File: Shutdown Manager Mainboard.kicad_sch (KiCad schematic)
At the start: 20 parts, among them J1 Conn_01x04, J2 Conn_01x03, J3 Conn_01x03, J6 Conn_01x03, K1 Relay_SPST_Panasonic_DJH-Form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, U1 Seeed Studio XIAO SAMD21, U2 TPS76133DBVR, U3 DRV8220DSGR, U4 DRV8220DSGR

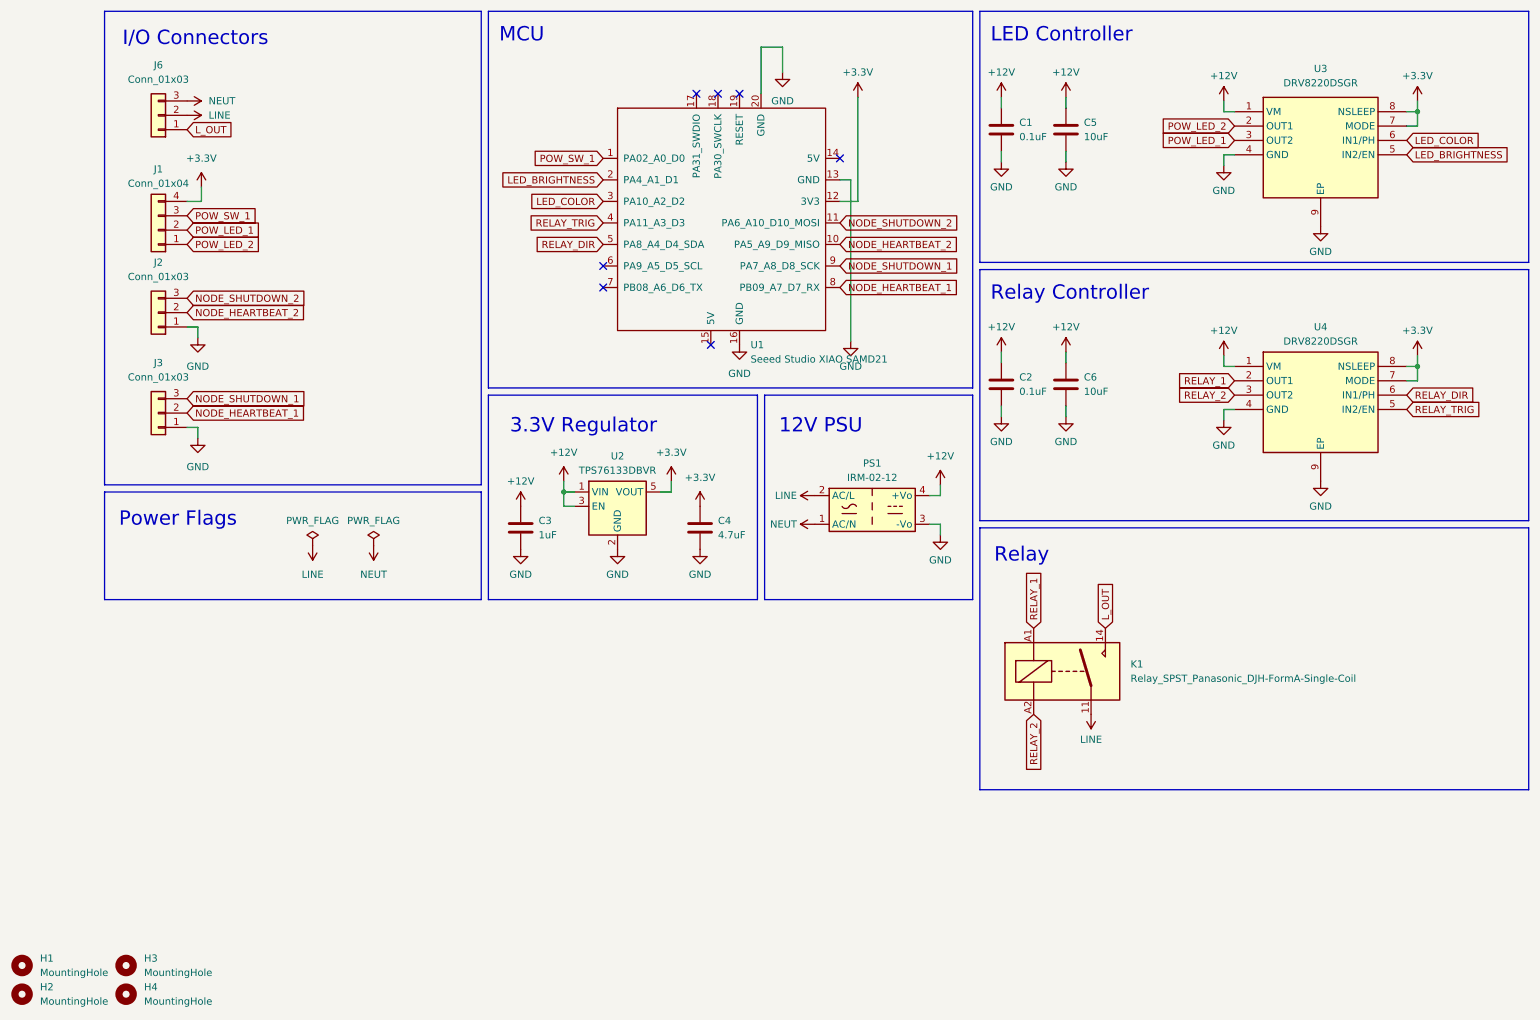
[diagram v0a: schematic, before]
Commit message: Added strong external pullup/-down resistors to inputs, Added RC filter to main power button input
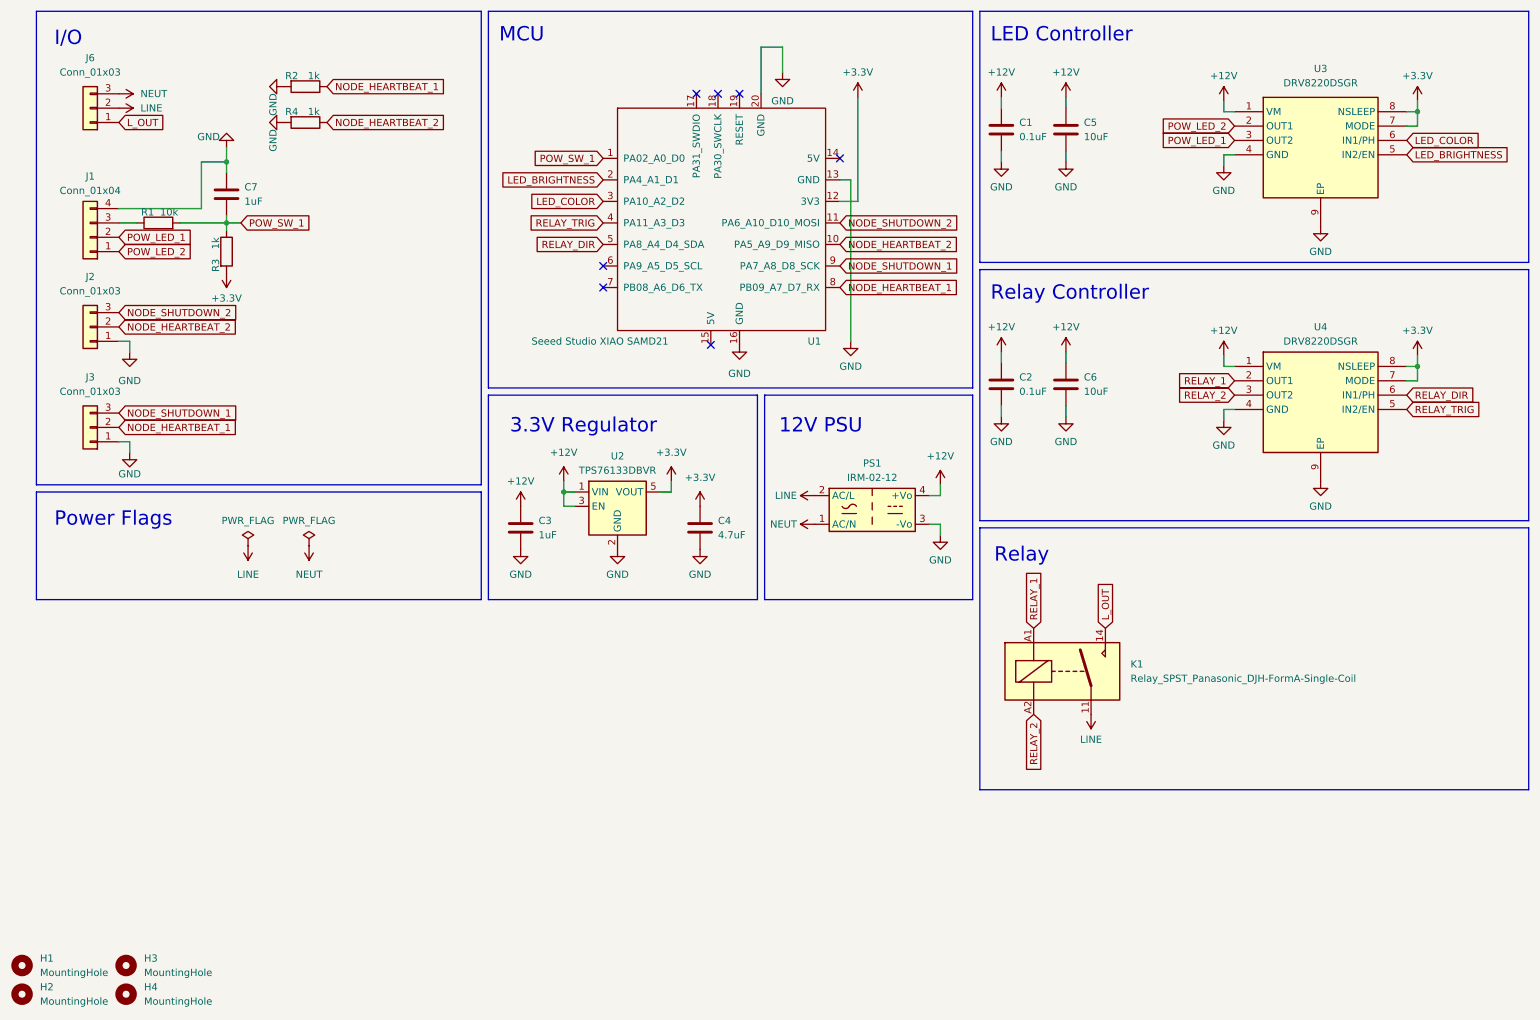
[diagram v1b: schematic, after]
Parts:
- added C7: 1uF, Capacitor_SMD:C_0402_1005Metric, symbol Device:C
- added R1: 10k, Resistor_SMD:R_0402_1005Metric, symbol Device:R
- added R2, R3, R4: 1k, Resistor_SMD:R_0402_1005Metric, symbol Device:R
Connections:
- net +3.3V: now also R3.2; no longer J1.4 (Pin_4)
- net GND: now also J1.4 (Pin_4), C7.1, R2.2, R4.2
- net NODE_HEARTBEAT_1: now also R2.1
- net NODE_HEARTBEAT_2: now also R4.1
- net POW_SW_1: now also C7.2, R1.2, R3.1; no longer J1.3 (Pin_3)
- new net: J1.3 (Pin_3), R1.1
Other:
- note added: "I/O"
- note removed: "I/O Connectors"
- moved on the sheet: J1, J2, J3, J6

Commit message: Fixed heartbeat input filtering
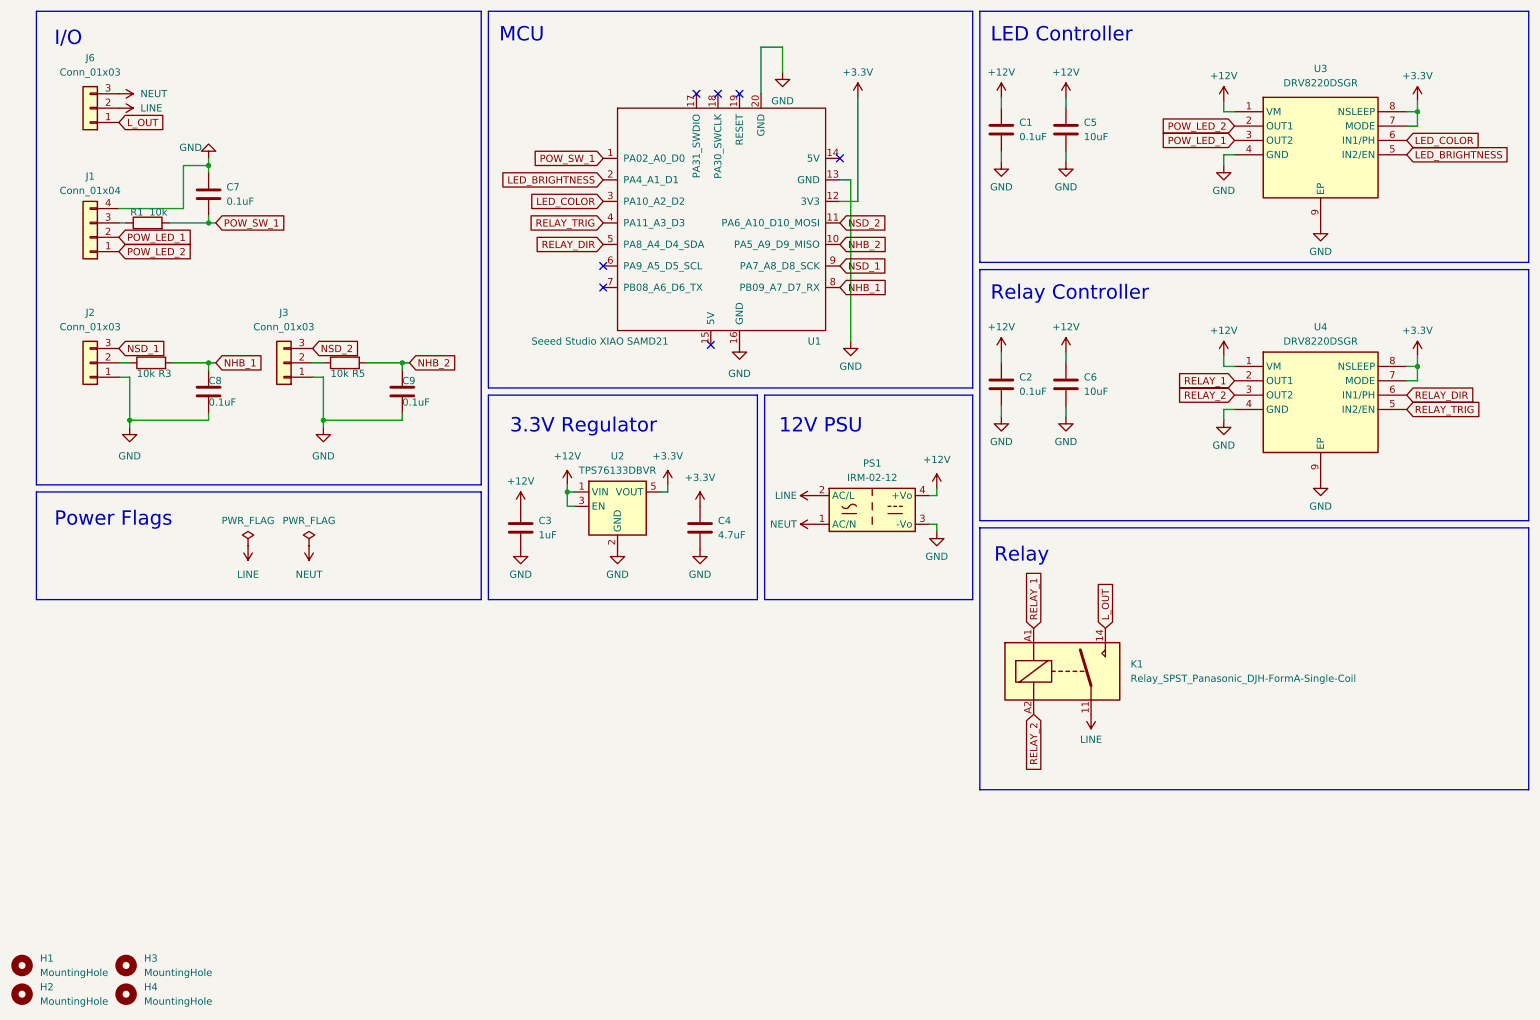
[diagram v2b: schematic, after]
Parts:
- removed R2, R4: 1k, Resistor_SMD:R_0402_1005Metric, symbol Device:R
- added C8, C9: 0.1uF, Capacitor_SMD:C_0402_1005Metric, symbol Device:C
- added R5: 10k, Resistor_SMD:R_0402_1005Metric, symbol Device:R
- C7: value 1uF -> 0.1uF; MPN C52923 -> C1525
- H1, H2, H3, H4: now left out of the parts list
- R3: value 1k -> 10k; MPN C11702 -> C25744
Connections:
- net +3.3V: no longer R3.2
- net GND: now also C8.2, C9.2
- net POW_SW_1: no longer R3.1
- net NODE_HEARTBEAT_1: no longer names the net of J3.2 (Pin_2)
- net NODE_HEARTBEAT_1: now also R5.1; no longer U1.8 (PB09_A7_D7_RX)
- net NODE_HEARTBEAT_2: no longer names the net of J2.2 (Pin_2)
- net NODE_HEARTBEAT_2: now also R3.1; no longer U1.10 (PA5_A9_D9_MISO)
- net NODE_SHUTDOWN_1 renamed NSD_1
- net NSD_1: now also J2.3 (Pin_3); no longer J3.3 (Pin_3)
- net NODE_SHUTDOWN_2 renamed NSD_2
- net NSD_2: now also J3.3 (Pin_3); no longer J2.3 (Pin_3)
- new net NHB_1: C8.1, R3.2, U1.8 (PB09_A7_D7_RX)
- new net NHB_2: C9.1, R5.2, U1.10 (PA5_A9_D9_MISO)
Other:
- moved on the sheet: C7, J2, J3, R1
